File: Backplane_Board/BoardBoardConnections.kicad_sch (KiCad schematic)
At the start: 0 parts

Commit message: added pico and 5v killSW
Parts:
- added D4, D6, D7: LED, symbol Device:LED
- added R22, R23, R24: 1K, symbol Device:R
- added U3: Pico, RPi_Pico:RPi_Pico_SMD_TH, symbol MCU_RaspberryPi_and_Boards:Pico
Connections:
- new net: R23.1, U3.21 (GPIO16)
- new net: D6.2 (A), R23.2
- new net: D4.2 (A), R22.2
- new net: R22.1, U3.25 (GPIO19)
- new net: R24.1, U3.29 (GPIO22)
- new net: D7.2 (A), R24.2
- new net +5V: U3.39 (VSYS)
- new net GND: D4.1 (K), D6.1 (K), D7.1 (K), U3.13 (GND), U3.18 (GND), U3.23 (GND), U3.28 (GND), U3.3 (GND), U3.33 (AGND), U3.38 (GND), U3.42 (GND), U3.8 (GND)
- new net RUN: U3.30 (RUN)
- new net SCL: U3.5 (GPIO3)
- new net SDA: U3.4 (GPIO2)
- new net SERVO0: U3.14 (GPIO10)
- new net SERVO1: U3.15 (GPIO11)
- new net SERVO2: U3.16 (GPIO12)
- new net SERVO24: U3.19 (GPIO14)
- new net SERVO3: U3.17 (GPIO13)
- new net SERVO5: U3.20 (GPIO15)
- new net SW0: U3.11 (GPIO8)
- new net SW1: U3.12 (GPIO9)
- new net SW2: U3.6 (GPIO4)
- new net SW3: U3.7 (GPIO5)
- new net SW4: U3.9 (GPIO6)
- new net SW5: U3.10 (GPIO7)
- new net SWCLK: U3.41 (SWCLK), U3.43 (SWDIO)
- new net UART(RX): U3.2 (GPIO1)
- new net UART(TX): U3.1 (GPIO0)
- no-connect marks 0 -> 11
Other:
- note added: "TODO: add shotkey diode on input for protection in the event of dull powering"

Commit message: added more pico stuff
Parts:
- added D9: MBR120VLSFT1G, symbol Device:D_Schottky
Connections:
- net +5V: now also D9.2 (A); no longer U3.39 (VSYS)
- new net: D9.1 (K), U3.39 (VSYS)
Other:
- moved on the sheet: D4, D6, D7, R22, R23, R24, U3

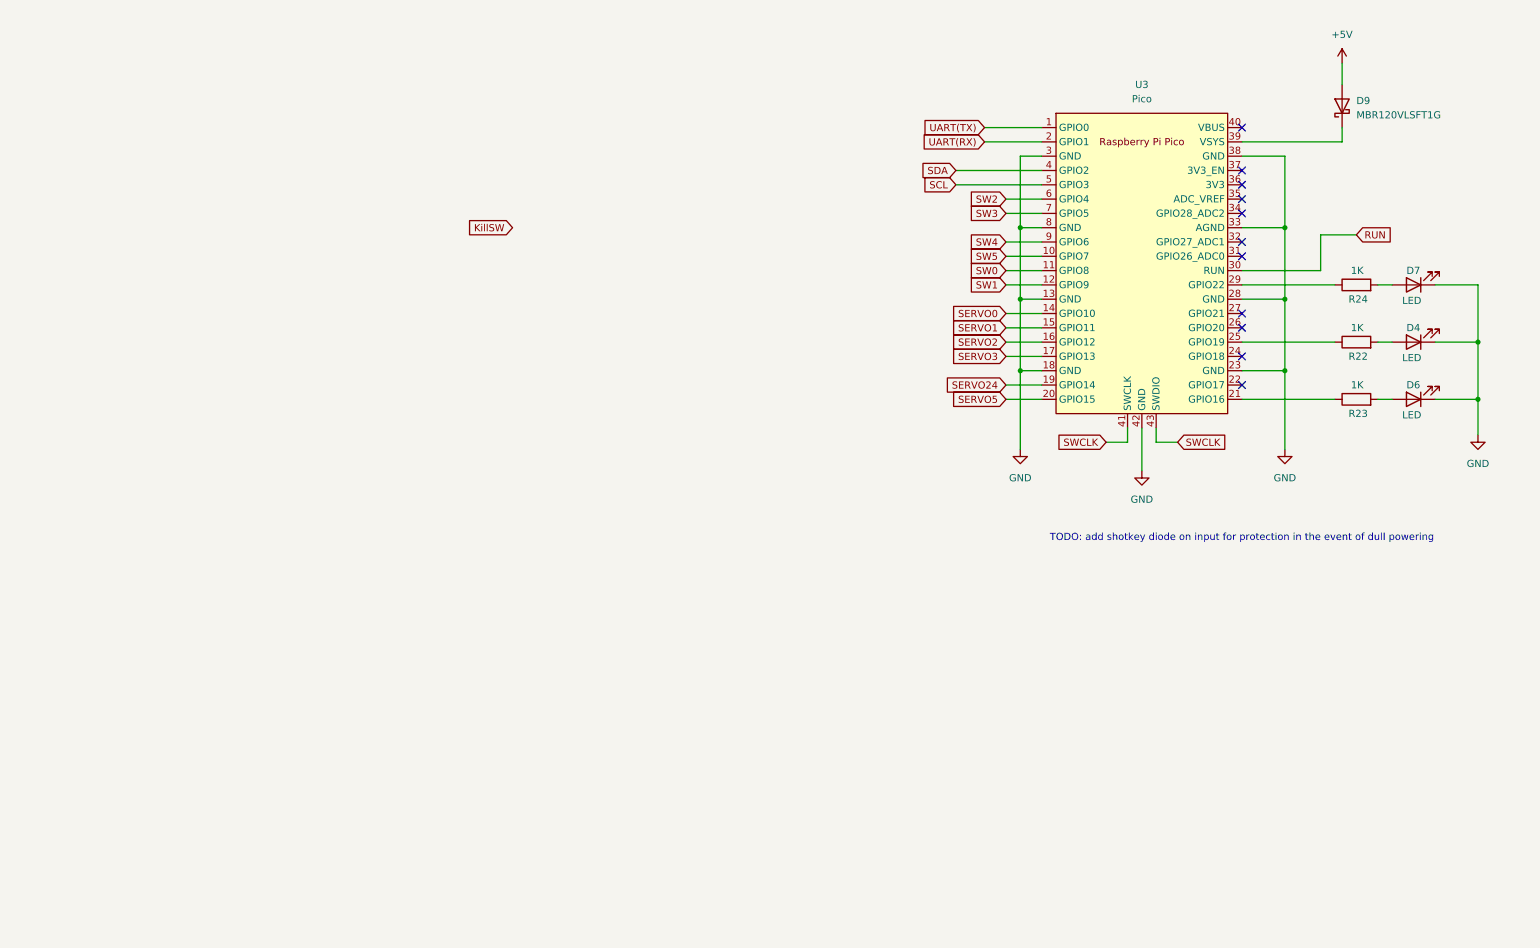
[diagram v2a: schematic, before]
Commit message: added power swtching circits
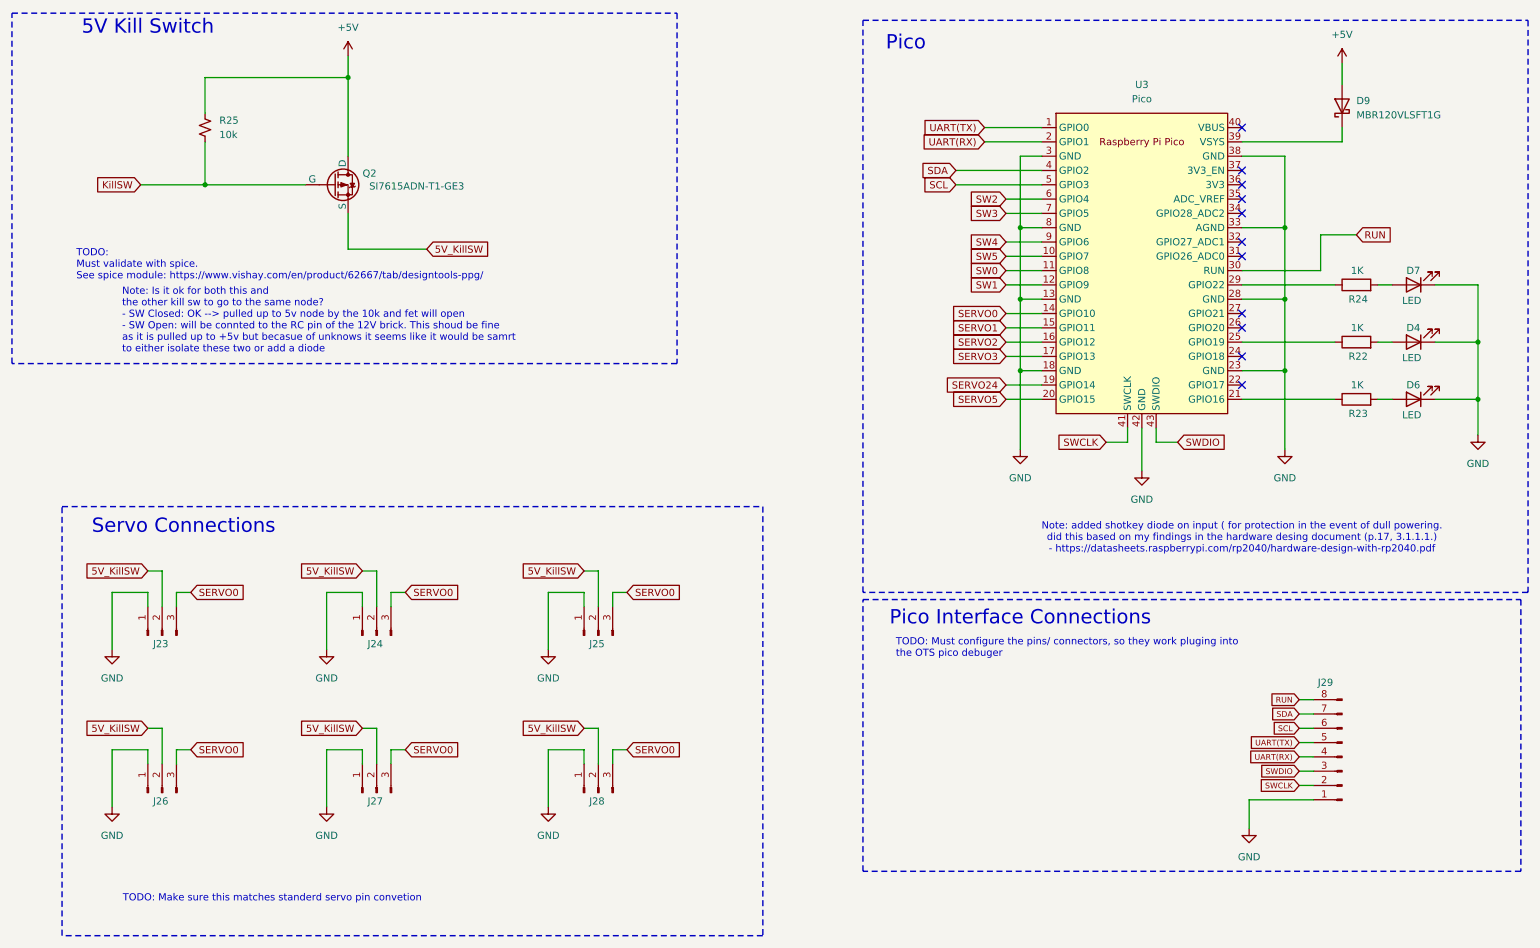
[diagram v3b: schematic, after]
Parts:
- added J23, J24, J25, J26, J27, J28: Conn_01x03_Pin, symbol Connector:Conn_01x03_Pin
- added J29: Conn_01x08_Pin, symbol Connector:Conn_01x08_Pin
- added Q2: SI7615ADN-T1-GE3, symbol Simulation_SPICE:PMOS
- added R25: 10k, symbol Device:R_Small_US
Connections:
- net +5V: now also Q2.1 (D), R25.1
- net GND: now also J23.1 (Pin_1), J24.1 (Pin_1), J25.1 (Pin_1), J26.1 (Pin_1), J27.1 (Pin_1), J28.1 (Pin_1), J29.1 (Pin_1)
- net KillSW: now also Q2.2 (G), R25.2
- net RUN: now also J29.8 (Pin_8)
- net SCL: now also J29.6 (Pin_6)
- net SDA: now also J29.7 (Pin_7)
- net SERVO0: now also J23.3 (Pin_3), J24.3 (Pin_3), J25.3 (Pin_3), J26.3 (Pin_3), J27.3 (Pin_3), J28.3 (Pin_3)
- net SWCLK: now also J29.2 (Pin_2); no longer U3.43 (SWDIO)
- net UART(RX): now also J29.4 (Pin_4)
- net UART(TX): now also J29.5 (Pin_5)
- new net 5V_KillSW: J23.2 (Pin_2), J24.2 (Pin_2), J25.2 (Pin_2), J26.2 (Pin_2), J27.2 (Pin_2), J28.2 (Pin_2), Q2.3 (S)
- new net SWDIO: J29.3 (Pin_3), U3.43 (SWDIO)
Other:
- note added: "5V Kill Switch"
- note added: "Note: Is it ok for both this and the other kill sw to go to the same node? - SW Closed: OK --> pulled up to 5v node by the 10k and fet will open - SW Open: will be connted to the RC pin of the 12V brick. This shoud be fine as it is pulled up to +5v but becasue of unknows it seems like it would be samrt to either isolate these two or add a diode"
- note added: "Note: added shotkey diode on input ( for protection in the event of dull powering. did this based on my findings in the hardware desing document (p.17, 3.1.1.1.) - https://datasheets.raspberrypi.com/rp2040/hardware-design-with-rp2040.pdf"
- note added: "Pico"
- note added: "Pico Interface Connections"
- note added: "Servo Connections"
- note added: "TODO: Make sure this matches standerd servo pin convetion"
- note added: "TODO: Must configure the pins/ connectors, so they work pluging into the OTS pico debuger"
- note added: "TODO: Must validate with spice. See spice module: https://www.vishay.com/en/product/62667/tab/designtools-ppg/"
- note removed: "TODO: add shotkey diode on input for protection in the event of dull powering"

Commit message: ready for final schmatic review
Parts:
- removed J29: Conn_01x08_Pin, symbol Connector:Conn_01x08_Pin
- added F10, F11, F12, F7, F8, F9: 0ZCG0300FF2B, symbol Device:Polyfuse
- added J29: Conn_01x05_Socket, symbol Connector:Conn_01x05_Socket
- added J36, J37: BM03B-SRSS-TB, Connector_JST:JST_SH_BM03B-SRSS-TB_1x03-1MP_P1.00mm_Vertical, symbol Connector:Conn_01x03_Socket
- U3: footprint RPi_Pico:RPi_Pico_SMD_TH -> MCU_RaspberryPi_and_Boards:RPi_Pico_SMD_TH
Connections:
- net +5V: now also J29.1 (Pin_1)
- net 5V_KillSW: now also F10.1, F11.1, F12.1, F7.1, F8.1, F9.1; no longer J23.2 (Pin_2), J24.2 (Pin_2), J25.2 (Pin_2), J26.2 (Pin_2), J27.2 (Pin_2), J28.2 (Pin_2)
- net GND: now also J29.5 (Pin_5), J36.2 (Pin_2), J37.2 (Pin_2)
- net RUN: now also J29.2 (Pin_2)
- net SCL: now also J29.4 (Pin_4)
- net SDA: now also J29.3 (Pin_3)
- net SWCLK: now also J37.3 (Pin_3)
- net SWDIO: now also J37.1 (Pin_1)
- net UART(RX): now also J36.1 (Pin_1)
- net UART(TX): now also J36.3 (Pin_3)
- net ALERT: now reaches U3.24 (GPIO18)
- net SERVO24 renamed SERVO4
- new net: F9.2, J25.2 (Pin_2)
- new net: F8.2, J24.2 (Pin_2)
- new net: F12.2, J28.2 (Pin_2)
- new net: F10.2, J26.2 (Pin_2)
- new net: F7.2, J23.2 (Pin_2)
- new net: F11.2, J27.2 (Pin_2)
- no-connect marks 11 -> 10
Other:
- note added: "TODO: Must configure the pins/ connectors, so they work pluging into the OTS pico debuger - https://datasheets.raspberrypi.com/debug/debug-connector-specification.pdf"
- note removed: "TODO: Must configure the pins/ connectors, so they work pluging into the OTS pico debuger"
- moved on the sheet: J23

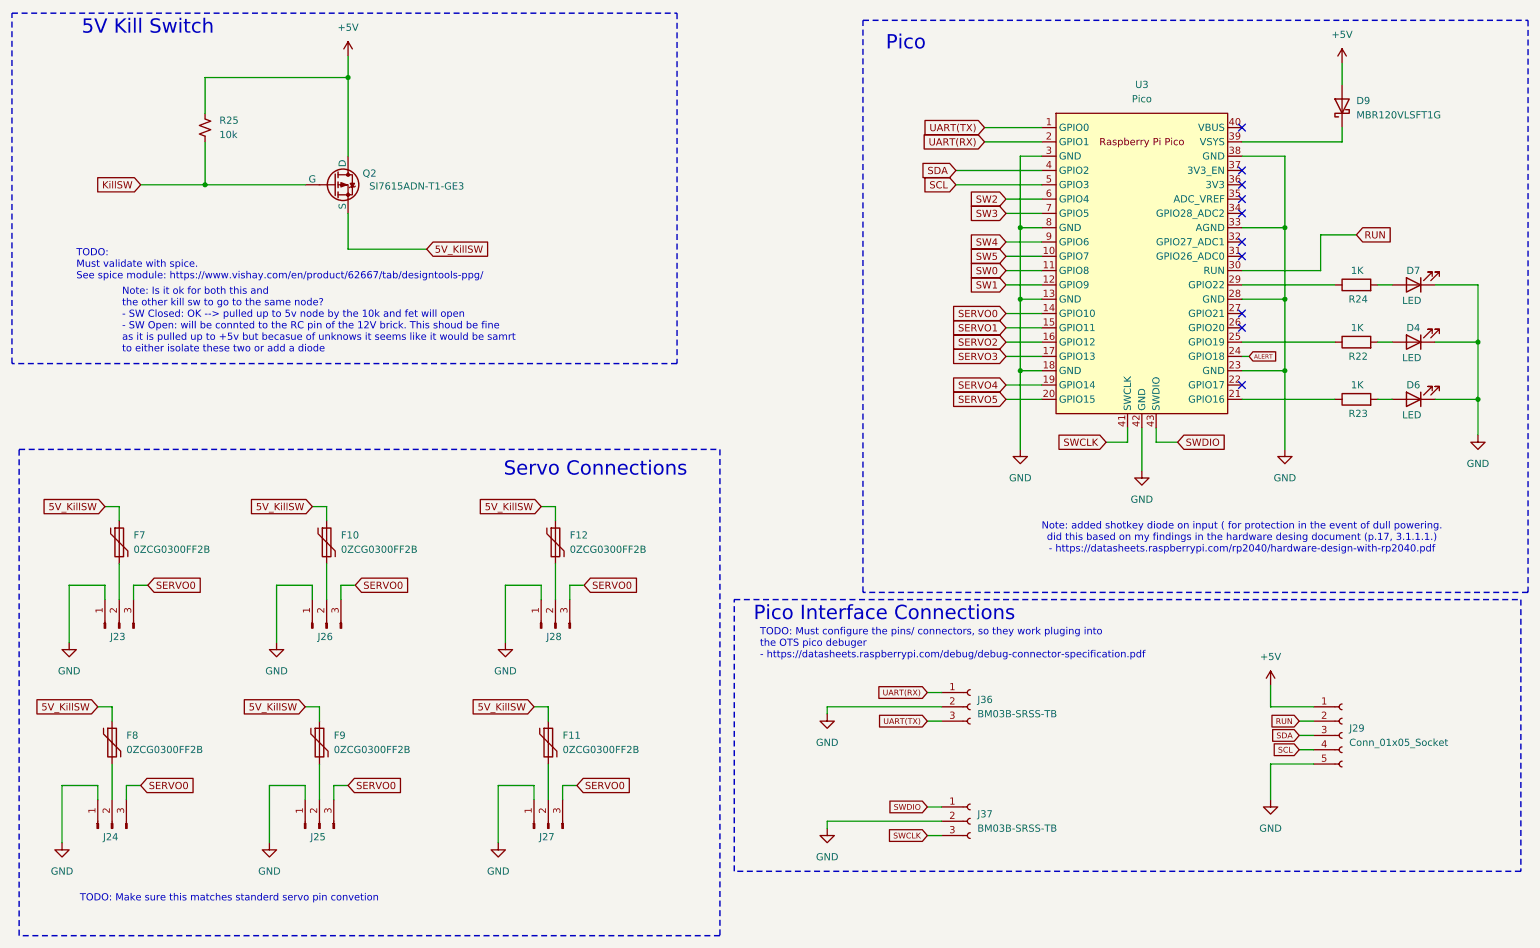
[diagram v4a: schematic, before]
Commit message: updated i2c pullups to 3V3 logic, not isolator needed
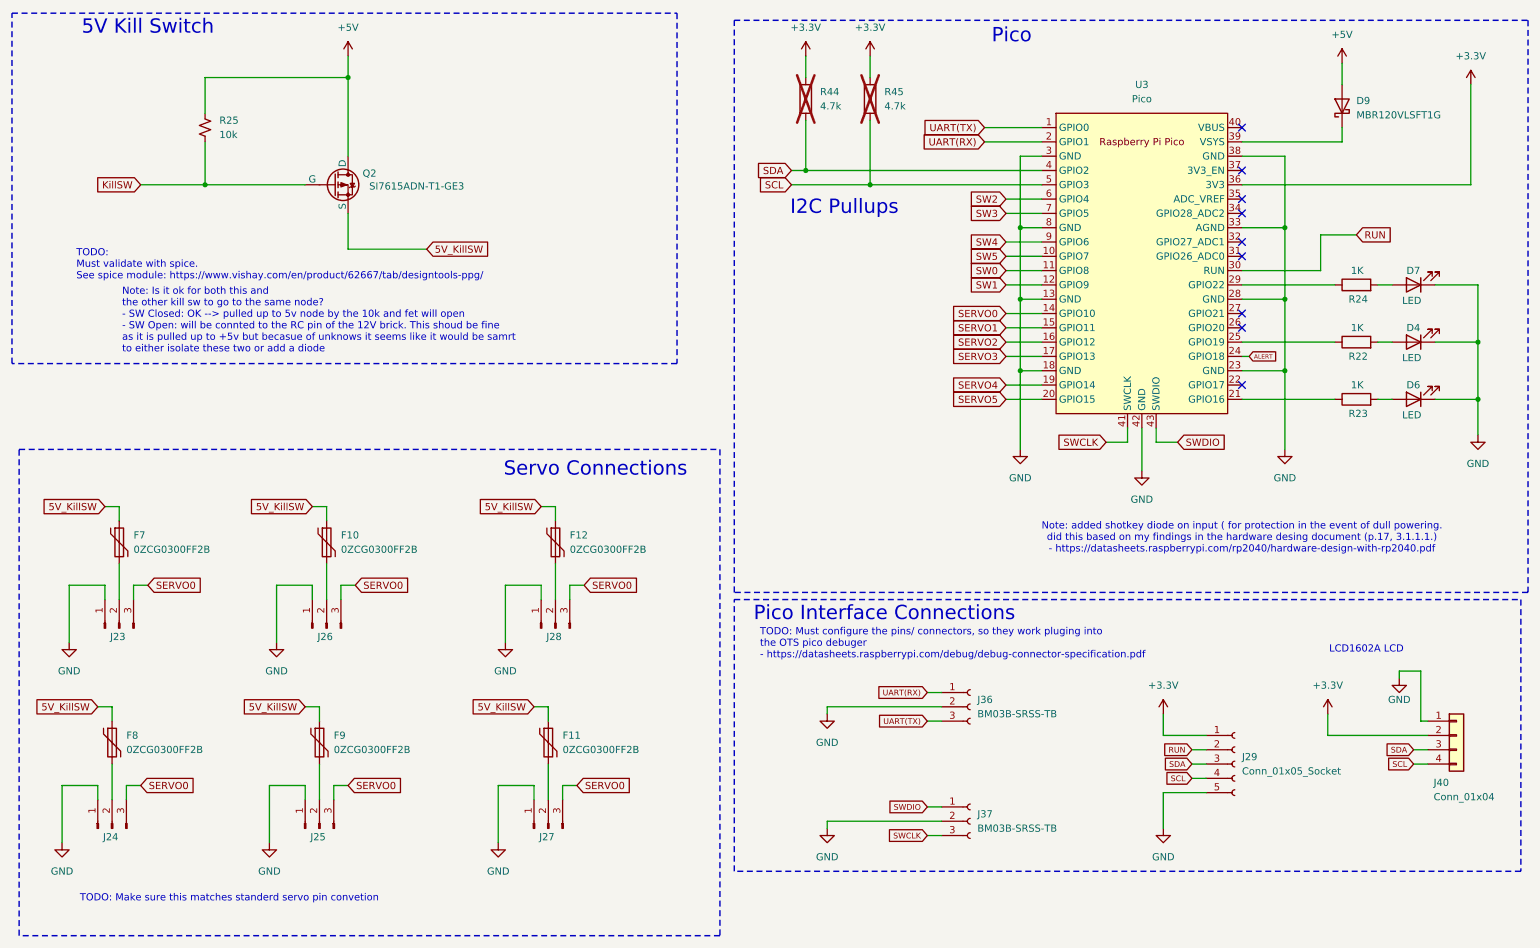
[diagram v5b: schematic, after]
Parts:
- added J40: Conn_01x04, symbol Connector_Generic:Conn_01x04
- added R44, R45: 4.7k, symbol Device:R
- Q2: footprint (none) -> SI7615ADN-T1-GE3:SON8_SI7615ADN-T1-GE3_VIS-L
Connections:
- net +5V: no longer J29.1 (Pin_1)
- net GND: now also J40.1 (Pin_1)
- net SCL: now also J40.4 (Pin_4), R45.2
- net SDA: now also J40.3 (Pin_3), R44.2
- net +3.3V: now reaches U3.36 (3V3)
- net +3.3V: now also J29.1 (Pin_1), J40.2 (Pin_2), R44.1, R45.1
- no-connect marks 10 -> 9
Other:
- note added: "I2C Pullups"
- note added: "LCD1602A LCD"
- moved on the sheet: J29

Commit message: update FET circits
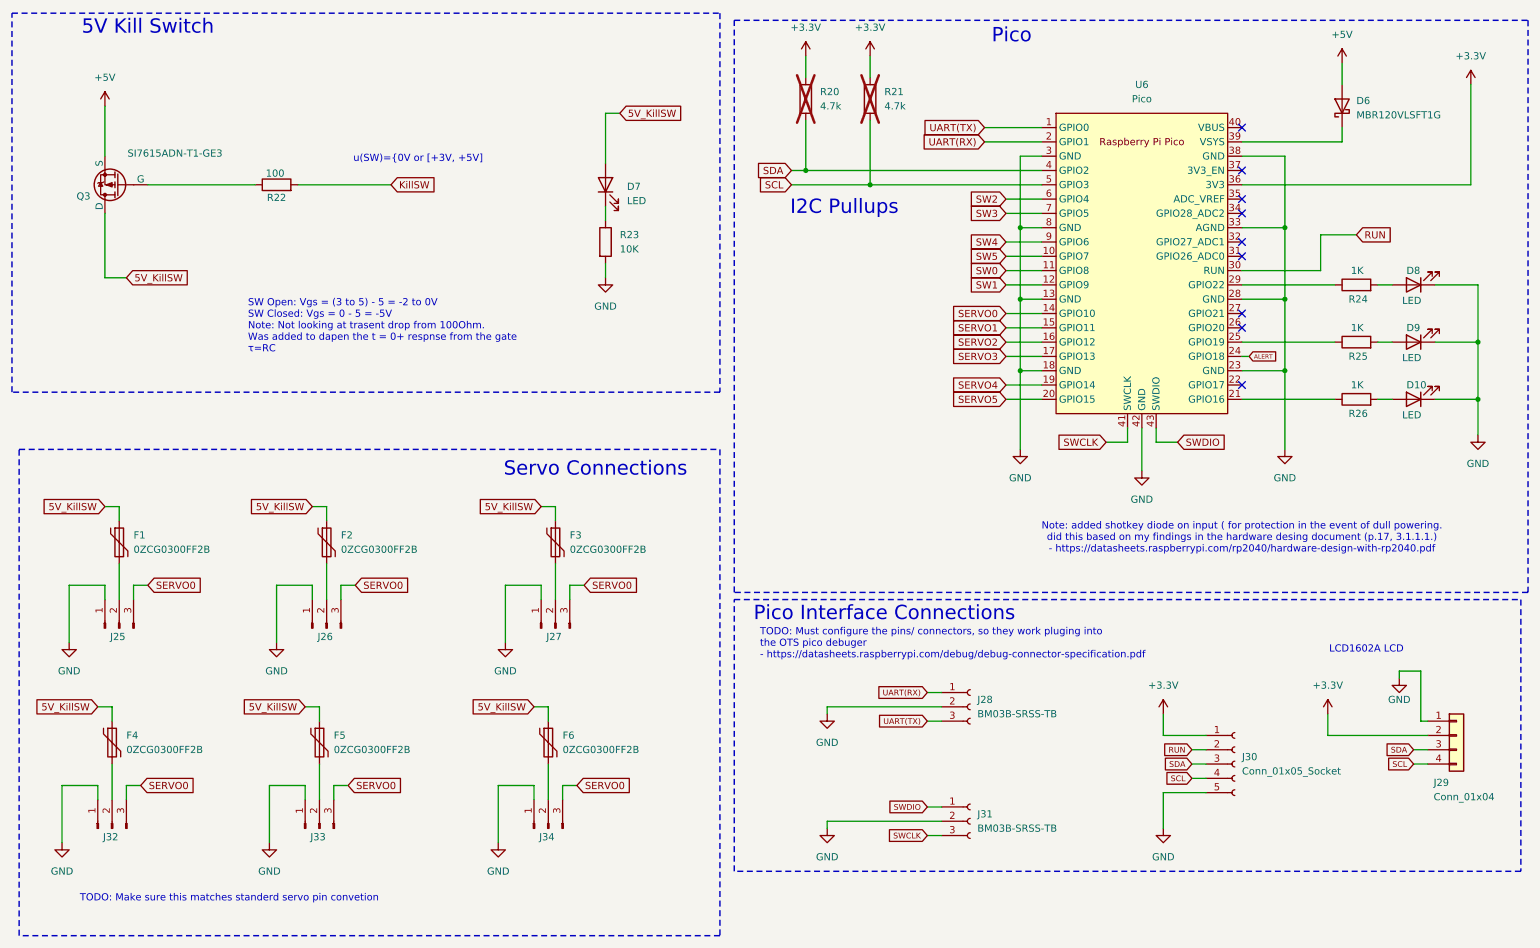
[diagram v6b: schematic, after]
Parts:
- removed R25: 10k, symbol Device:R_Small_US
- added D7: LED, symbol Device:LED
- added R22: 100, symbol Device:R
- added R23: 10K, symbol Device:R
- F1: renamed from F7; footprint (none) -> Fuse:Fuse_1812_4532Metric
- F2: renamed from F10; footprint (none) -> Fuse:Fuse_1812_4532Metric
- F3: renamed from F12; footprint (none) -> Fuse:Fuse_1812_4532Metric
- F4: renamed from F8; footprint (none) -> Fuse:Fuse_1812_4532Metric
- F5: renamed from F9; footprint (none) -> Fuse:Fuse_1812_4532Metric
- F6: renamed from F11; footprint (none) -> Fuse:Fuse_1812_4532Metric
- renumbered D6 to D10, D9 to D6, D7 to D8, D4 to D9, J23 to J25, J28 to J27, J36 to J28, J40 to J29, J29 to J30, J37 to J31, J24 to J32, J25 to J33, J27 to J34, Q2 to Q3, R44 to R20, R45 to R21, R22 to R25, R23 to R26, U3 to U6
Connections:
- net +5V: now also Q3.3 (S); no longer Q3.1 (D)
- net 5V_KillSW: now also Q3.1 (D), D7.2 (A); no longer Q3.3 (S)
- net GND: now also R23.2
- net KillSW: now also R22.2; no longer Q3.2 (G)
- new net: D7.1 (K), R23.1
- new net: Q3.2 (G), R22.1
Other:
- note added: "SW Open: Vgs = (3 to 5) - 5 = -2 to 0V SW Closed: Vgs = 0 - 5 = -5V Note: Not looking at trasent drop from 100Ohm. Was added to dapen the t = 0+ respnse from the gate τ=RC"
- note added: "u(SW)={0V or [+3V, +5V]"
- note removed: "Note: Is it ok for both this and the other kill sw to go to the same node? - SW Closed: OK --> pulled up to 5v node by the 10k and fet will open - SW Open: will be connted to the RC pin of the 12V brick. This shoud be fine as it is pulled up to +5v but becasue of unknows it seems like it would be samrt to either isolate these two or add a diode"
- note removed: "TODO: Must validate with spice. See spice module: https://www.vishay.com/en/product/62667/tab/designtools-ppg/"
- moved on the sheet: Q3
